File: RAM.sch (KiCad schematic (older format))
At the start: 2 parts, among them U2 AS4C256M16D3LC-12BCN, U3 AS4C256M16D3LC-12BCN

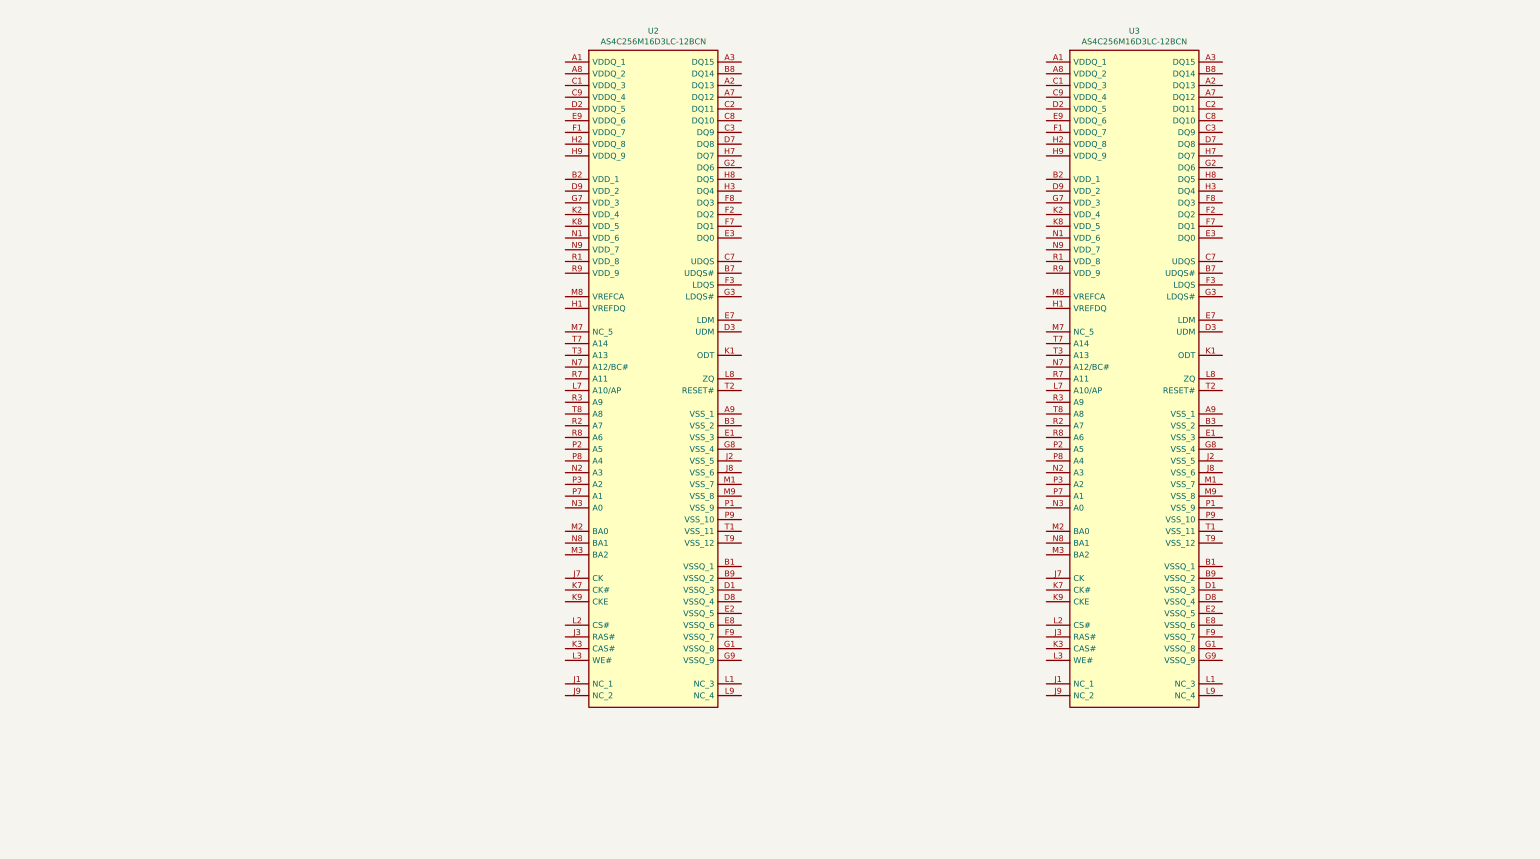
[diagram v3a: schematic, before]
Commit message: Drawn schematic RAM
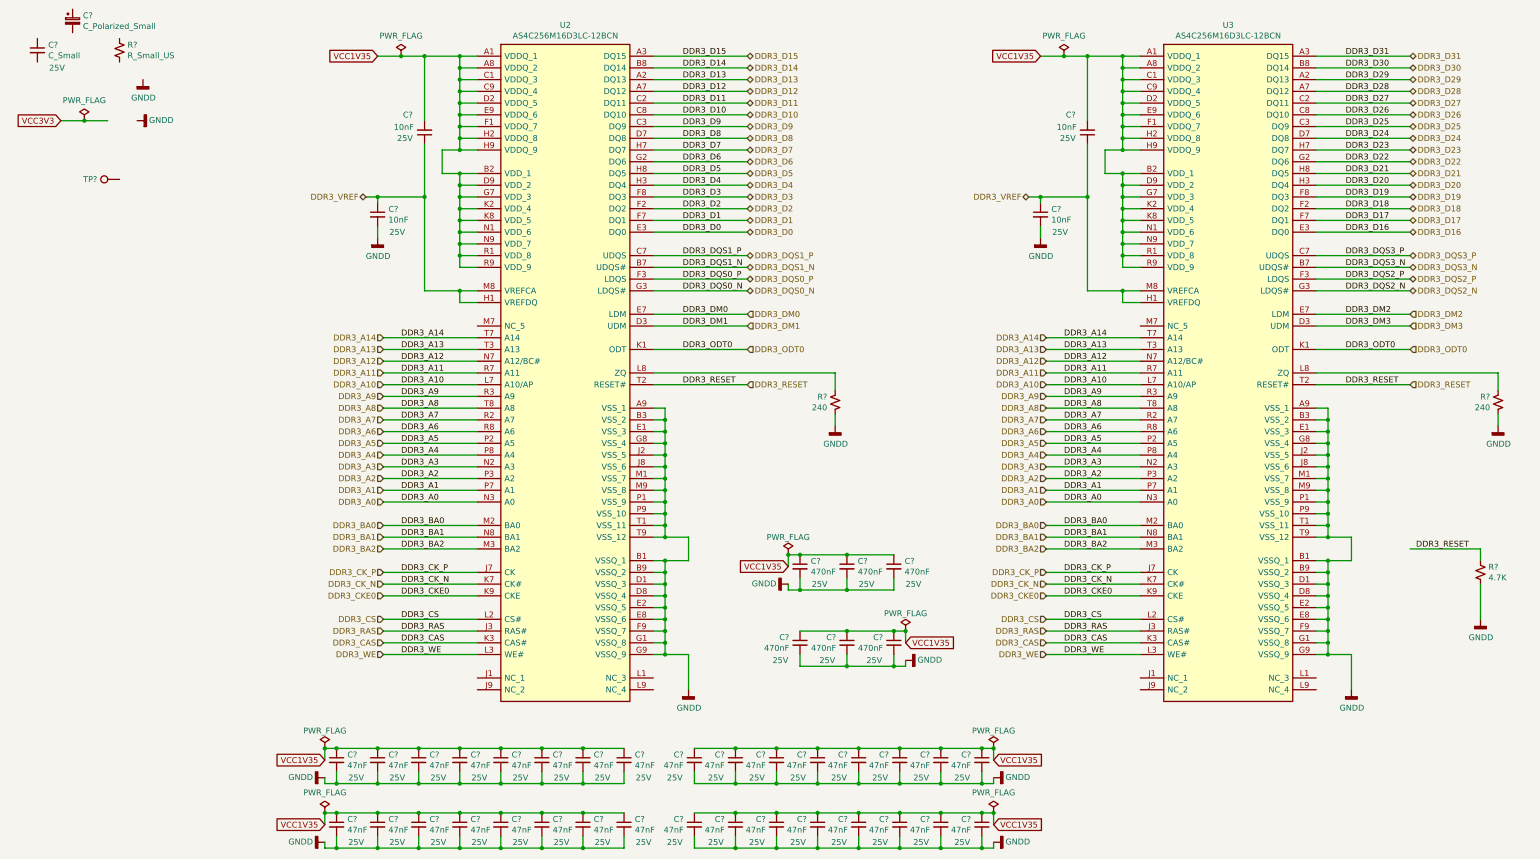
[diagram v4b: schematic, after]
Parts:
- added C?: C_Polarized_Small, Capacitor_Tantalum_SMD:CP_EIA-1608-10_AVX-L_Pad1.25x1.05mm_HandSolder, symbol Device:C_Polarized_Small
- added C?: C_Small, Capacitor_SMD:C_0603_1608Metric_Pad1.08x0.95mm_HandSolder, symbol Device:C_Small
- added C? (x4): 10nF, Capacitor_SMD:C_0603_1608Metric_Pad1.08x0.95mm_HandSolder, symbol Device:C_Small
- added C? (x32): 47nF, Capacitor_SMD:C_0603_1608Metric_Pad1.08x0.95mm_HandSolder, symbol Device:C_Small
- added C? (x6): 470nF, Capacitor_SMD:C_0603_1608Metric_Pad1.08x0.95mm_HandSolder, symbol Device:C_Small
- added R?: R_Small_US, Resistor_SMD:R_0603_1608Metric_Pad0.98x0.95mm_HandSolder, symbol Device:R_Small_US
- added R? (x2): 240, Resistor_SMD:R_0603_1608Metric_Pad0.98x0.95mm_HandSolder, symbol Device:R_Small_US
- added R?: 4.7K, Resistor_SMD:R_0603_1608Metric_Pad0.98x0.95mm_HandSolder, symbol Device:R_Small_US
- added TP?: TestPoint, TestPoint:TestPoint_Pad_D1.5mm, symbol Connector:TestPoint
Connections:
- net VCC1V35: now reaches U2.A1 (VDDQ_1)
- net VCC1V35: now also U2.A8 (VDDQ_2), U2.B2 (VDD_1), U2.C1 (VDDQ_3), U2.C9 (VDDQ_4), U2.D2 (VDDQ_5), U2.D9 (VDD_2), U2.E9 (VDDQ_6), U2.F1 (VDDQ_7), U2.G7 (VDD_3), U2.H2 (VDDQ_8), U2.H9 (VDDQ_9), U2.K2 (VDD_4), U2.K8 (VDD_5), U2.N1 (VDD_6), U2.N9 (VDD_7), U2.R1 (VDD_8), U2.R9 (VDD_9), U3.A1 (VDDQ_1), U3.A8 (VDDQ_2), U3.B2 (VDD_1), U3.C1 (VDDQ_3), U3.C9 (VDDQ_4), U3.D2 (VDDQ_5), U3.D9 (VDD_2), U3.E9 (VDDQ_6), U3.F1 (VDDQ_7), U3.G7 (VDD_3), U3.H2 (VDDQ_8), U3.H9 (VDDQ_9), U3.K2 (VDD_4), U3.K8 (VDD_5), U3.N1 (VDD_6), U3.N9 (VDD_7), U3.R1 (VDD_8), U3.R9 (VDD_9), C?.1, C?.1, C?.1, C?.1, C?.1, C?.1, C?.1, C?.1, C?.1, C?.1, C?.1, C?.1, C?.1, C?.1, C?.1, C?.1, C?.1, C?.1, C?.1, C?.1, C?.1, C?.1, C?.1, C?.1, C?.1, C?.1, C?.1, C?.1, C?.1, C?.1, C?.1, C?.1, C?.1, C?.1, C?.1, C?.1, C?.1, C?.1, C?.2, C?.2
- net DDR3_D13: now reaches U2.A2 (DQ13)
- net DDR3_D15: now reaches U2.A3 (DQ15)
- net DDR3_D12: now reaches U2.A7 (DQ12)
- net GNDD: now reaches U2.A9 (VSS_1)
- net GNDD: now also U2.B1 (VSSQ_1), U2.B3 (VSS_2), U2.B9 (VSSQ_2), U2.D1 (VSSQ_3), U2.D8 (VSSQ_4), U2.E1 (VSS_3), U2.E2 (VSSQ_5), U2.E8 (VSSQ_6), U2.F9 (VSSQ_7), U2.G1 (VSSQ_8), U2.G8 (VSS_4), U2.G9 (VSSQ_9), U2.J2 (VSS_5), U2.J8 (VSS_6), U2.M1 (VSS_7), U2.M9 (VSS_8), U2.P1 (VSS_9), U2.P9 (VSS_10), U2.T1 (VSS_11), U2.T9 (VSS_12), U3.A9 (VSS_1), U3.B1 (VSSQ_1), U3.B3 (VSS_2), U3.B9 (VSSQ_2), U3.D1 (VSSQ_3), U3.D8 (VSSQ_4), U3.E1 (VSS_3), U3.E2 (VSSQ_5), U3.E8 (VSSQ_6), U3.F9 (VSSQ_7), U3.G1 (VSSQ_8), U3.G8 (VSS_4), U3.G9 (VSSQ_9), U3.J2 (VSS_5), U3.J8 (VSS_6), U3.M1 (VSS_7), U3.M9 (VSS_8), U3.P1 (VSS_9), U3.P9 (VSS_10), U3.T1 (VSS_11), U3.T9 (VSS_12), C?.2, C?.2, C?.2, C?.2, C?.2, C?.2, C?.2, C?.2, C?.2, C?.2, C?.2, C?.2, C?.2, C?.2, C?.2, C?.2, C?.2, C?.2, C?.2, C?.2, C?.2, C?.2, C?.2, C?.2, C?.2, C?.2, C?.2, C?.2, C?.2, C?.2, C?.2, C?.2, C?.2, C?.2, C?.2, C?.2, C?.2, C?.2, C?.2, C?.2, R?.2, R?.2, R?.2
- net DDR3_DQS1_N: now reaches U2.B7 (UDQS#)
- net DDR3_D14: now reaches U2.B8 (DQ14)
- net DDR3_D11: now reaches U2.C2 (DQ11)
- net DDR3_D9: now reaches U2.C3 (DQ9)
- net DDR3_DQS1_P: now reaches U2.C7 (UDQS)
- net DDR3_D10: now reaches U2.C8 (DQ10)
- net DDR3_DM1: now reaches U2.D3 (UDM)
- net DDR3_D8: now reaches U2.D7 (DQ8)
- net DDR3_D0: now reaches U2.E3 (DQ0)
- net DDR3_DM0: now reaches U2.E7 (LDM)
- net DDR3_D2: now reaches U2.F2 (DQ2)
- net DDR3_DQS0_P: now reaches U2.F3 (LDQS)
- net DDR3_D1: now reaches U2.F7 (DQ1)
- net DDR3_D3: now reaches U2.F8 (DQ3)
- net DDR3_D6: now reaches U2.G2 (DQ6)
- net DDR3_DQS0_N: now reaches U2.G3 (LDQS#)
- net DDR3_VREF: now reaches U2.H1 (VREFDQ)
- net DDR3_VREF: now also U2.M8 (VREFCA), U3.H1 (VREFDQ), U3.M8 (VREFCA), C?.1, C?.1, C?.1, C?.1
- net DDR3_D4: now reaches U2.H3 (DQ4)
- net DDR3_D7: now reaches U2.H7 (DQ7)
- net DDR3_D5: now reaches U2.H8 (DQ5)
- net DDR3_RAS: now reaches U2.J3 (RAS#)
- net DDR3_RAS: now also U3.J3 (RAS#)
- net DDR3_CK_P: now reaches U2.J7 (CK)
- net DDR3_CK_P: now also U3.J7 (CK)
- net DDR3_ODT0: now reaches U2.K1 (ODT)
- net DDR3_ODT0: now also U3.K1 (ODT)
- net DDR3_CAS: now reaches U2.K3 (CAS#)
- net DDR3_CAS: now also U3.K3 (CAS#)
- net DDR3_CK_N: now reaches U2.K7 (CK#)
- net DDR3_CK_N: now also U3.K7 (CK#)
- net DDR3_CKE0: now reaches U2.K9 (CKE)
- net DDR3_CKE0: now also U3.K9 (CKE)
- net DDR3_CS: now reaches U2.L2 (CS#)
- net DDR3_CS: now also U3.L2 (CS#)
- net DDR3_WE: now reaches U2.L3 (WE#)
- net DDR3_WE: now also U3.L3 (WE#)
- net DDR3_A10: now reaches U2.L7 (A10/AP)
- net DDR3_A10: now also U3.L7 (A10/AP)
- net at U2.L8 (ZQ): now also R?.1
- net DDR3_BA0: now reaches U2.M2 (BA0)
- net DDR3_BA0: now also U3.M2 (BA0)
- net DDR3_BA2: now reaches U2.M3 (BA2)
- net DDR3_BA2: now also U3.M3 (BA2)
- net DDR3_A3: now reaches U2.N2 (A3)
- net DDR3_A3: now also U3.N2 (A3)
- net DDR3_A0: now reaches U2.N3 (A0)
- net DDR3_A0: now also U3.N3 (A0)
- net DDR3_A12: now reaches U2.N7 (A12/BC#)
- net DDR3_A12: now also U3.N7 (A12/BC#)
- net DDR3_BA1: now reaches U2.N8 (BA1)
- net DDR3_BA1: now also U3.N8 (BA1)
- net DDR3_A5: now reaches U2.P2 (A5)
- net DDR3_A5: now also U3.P2 (A5)
- net DDR3_A2: now reaches U2.P3 (A2)
- net DDR3_A2: now also U3.P3 (A2)
- net DDR3_A1: now reaches U2.P7 (A1)
- net DDR3_A1: now also U3.P7 (A1)
- net DDR3_A4: now reaches U2.P8 (A4)
- net DDR3_A4: now also U3.P8 (A4)
- net DDR3_A7: now reaches U2.R2 (A7)
- net DDR3_A7: now also U3.R2 (A7)
- net DDR3_A9: now reaches U2.R3 (A9)
- net DDR3_A9: now also U3.R3 (A9)
- net DDR3_A11: now reaches U2.R7 (A11)
- net DDR3_A11: now also U3.R7 (A11)
- net DDR3_A6: now reaches U2.R8 (A6)
- net DDR3_A6: now also U3.R8 (A6)
- net DDR3_RESET: now reaches U2.T2 (RESET#)
- net DDR3_RESET: now also U3.T2 (RESET#), R?.1
- net DDR3_A13: now reaches U2.T3 (A13)
- net DDR3_A13: now also U3.T3 (A13)
- net DDR3_A14: now reaches U2.T7 (A14)
- net DDR3_A14: now also U3.T7 (A14)
- net DDR3_A8: now reaches U2.T8 (A8)
- net DDR3_A8: now also U3.T8 (A8)
- net DDR3_D29: now reaches U3.A2 (DQ13)
- net DDR3_D31: now reaches U3.A3 (DQ15)
- net DDR3_D28: now reaches U3.A7 (DQ12)
- net DDR3_DQS3_N: now reaches U3.B7 (UDQS#)
- net DDR3_D30: now reaches U3.B8 (DQ14)
- net DDR3_D27: now reaches U3.C2 (DQ11)
- net DDR3_D25: now reaches U3.C3 (DQ9)
- net DDR3_DQS3_P: now reaches U3.C7 (UDQS)
- net DDR3_D26: now reaches U3.C8 (DQ10)
- net DDR3_DM3: now reaches U3.D3 (UDM)
- net DDR3_D24: now reaches U3.D7 (DQ8)
- net DDR3_D16: now reaches U3.E3 (DQ0)
- net DDR3_DM2: now reaches U3.E7 (LDM)
- net DDR3_D18: now reaches U3.F2 (DQ2)
- net DDR3_DQS2_P: now reaches U3.F3 (LDQS)
- net DDR3_D17: now reaches U3.F7 (DQ1)
- net DDR3_D19: now reaches U3.F8 (DQ3)
- net DDR3_D22: now reaches U3.G2 (DQ6)
- net DDR3_DQS2_N: now reaches U3.G3 (LDQS#)
- net DDR3_D20: now reaches U3.H3 (DQ4)
- net DDR3_D23: now reaches U3.H7 (DQ7)
- net DDR3_D21: now reaches U3.H8 (DQ5)
- net at U3.L8 (ZQ): now also R?.1
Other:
- moved on the sheet: U2, U3

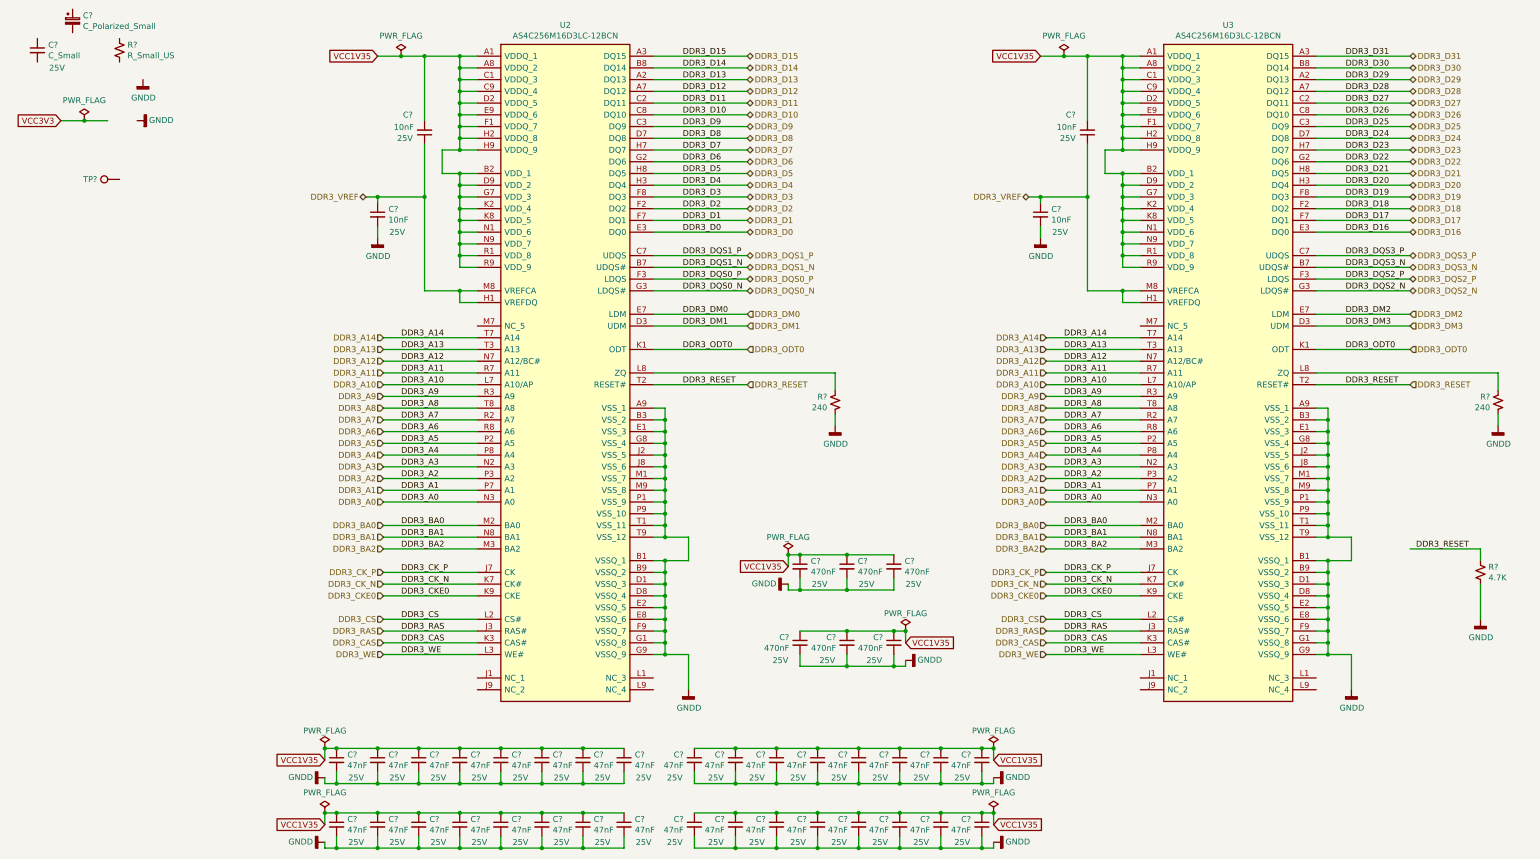
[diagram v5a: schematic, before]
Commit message: Added bus lines -ETH_PHY_CONN -RAM -USB2 Made Output the port direction of clkout of Clock_Gen Placed sheet entris of sheet symbols on top sheet
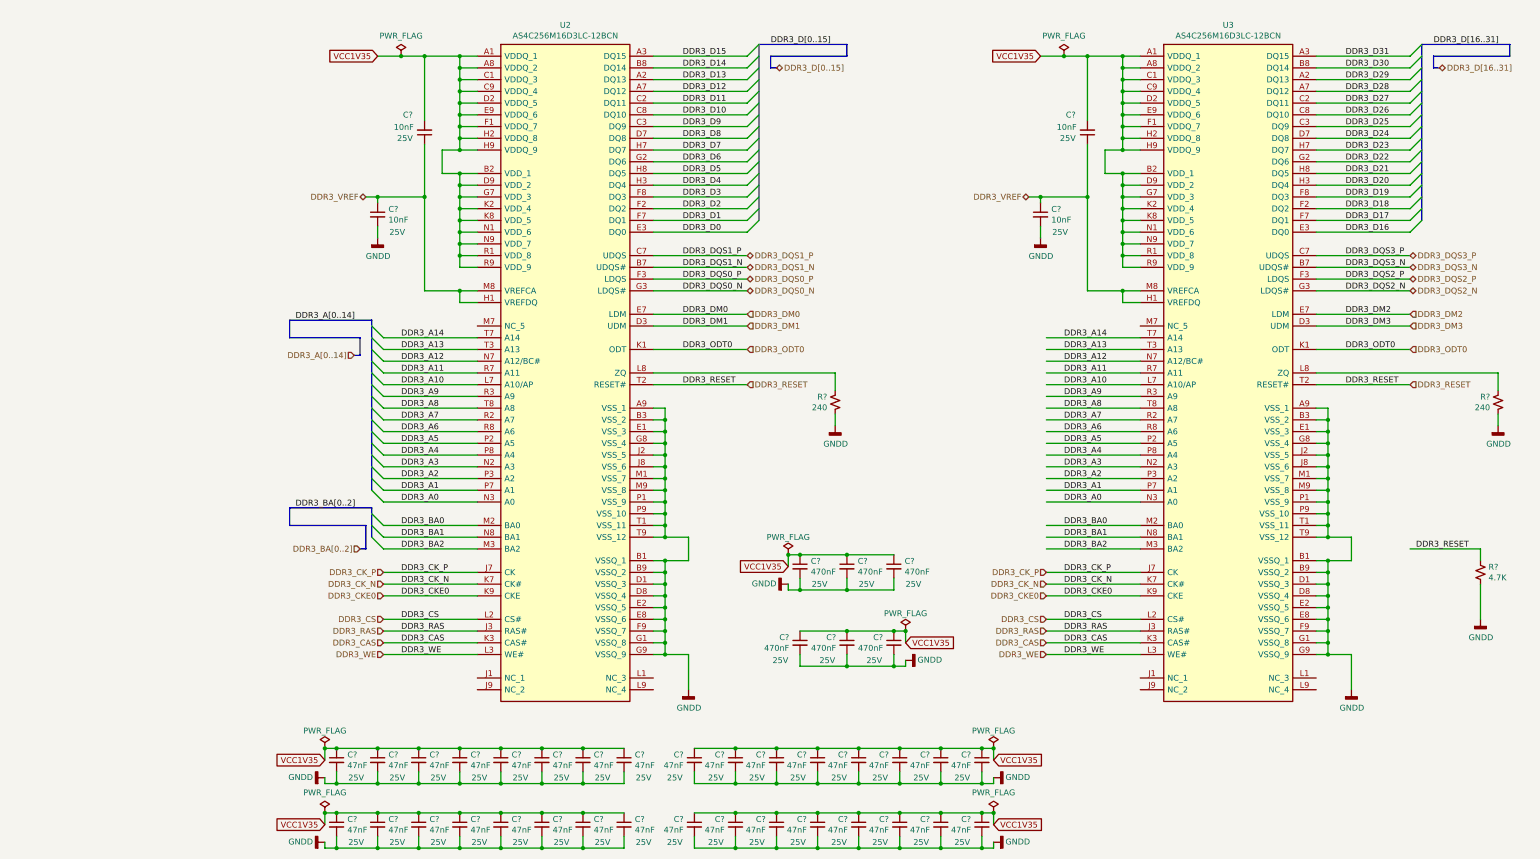
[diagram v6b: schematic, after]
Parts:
- removed C?: C_Polarized_Small, Capacitor_Tantalum_SMD:CP_EIA-1608-10_AVX-L_Pad1.25x1.05mm_HandSolder, symbol Device:C_Polarized_Small
- removed C?: C_Small, Capacitor_SMD:C_0603_1608Metric_Pad1.08x0.95mm_HandSolder, symbol Device:C_Small
- removed R?: R_Small_US, Resistor_SMD:R_0603_1608Metric_Pad0.98x0.95mm_HandSolder, symbol Device:R_Small_US
- removed TP?: TestPoint, TestPoint:TestPoint_Pad_D1.5mm, symbol Connector:TestPoint
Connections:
- net labels added: DDR3_A[0..14], DDR3_BA[0..2], DDR3_D[0..15], DDR3_D[16..31]
- net labels removed: VCC3V3
- wire segments 427 -> 425
